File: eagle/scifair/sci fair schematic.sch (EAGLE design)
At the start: 19 parts, among them IC1 LM555N, IC2 LM340H-12, Q1 BC817-16W, Q2 BC817-16W, X1 RIGHT, X2 LEFT, X3 PWR

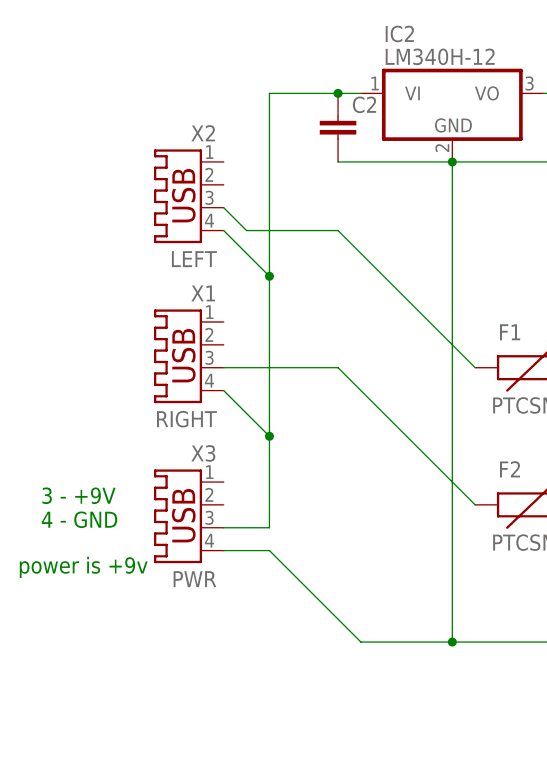
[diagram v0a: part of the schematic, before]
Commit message: Rework USB connections to use Sparkfun breakouts due to resource unavailability
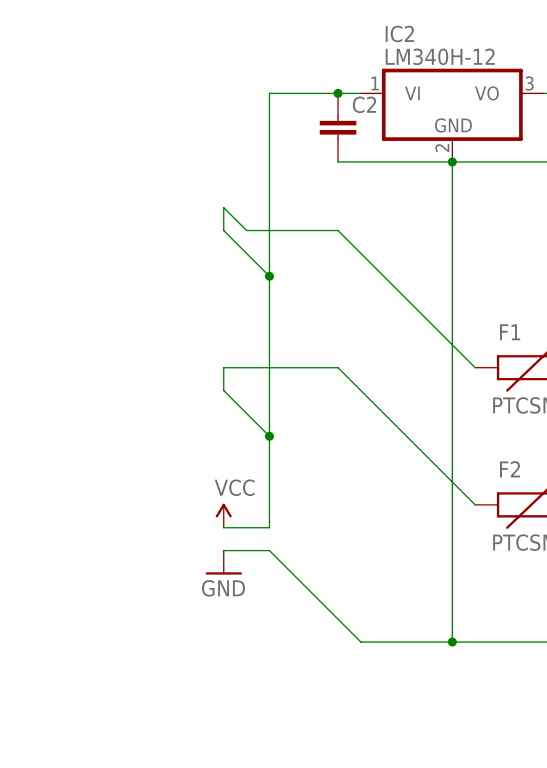
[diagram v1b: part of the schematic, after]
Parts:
- removed X1: RIGHT, con-yamaichi:USB-A003
- removed X2: LEFT, con-yamaichi:USB-A003
- removed X3: PWR, con-yamaichi:USB-A003
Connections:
- net N$6 renamed 5V
- removed net N$1: C2.1, IC2.VI, X1.4, X2.4, X3.3
- removed net N$2: F1.1, X2.3
- removed net N$3: F2.1, X1.3
- new net VCC: C2.1, F1.1, F2.1, IC2.VI
- net GND: no longer X3.4
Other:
- note removed: "3 - +9V 4 - GND"
- note removed: "power is +9v"
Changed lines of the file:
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@@
 <part name="Q1" library="semicon-smd-ipc" deviceset="NPN-TRANSISTOR_" device="SOT23" value="BC817-16W"/>
 <part name="Q2" library="semicon-smd-ipc" deviceset="NPN-TRANSISTOR_" device="SOT23" value="BC817-16W"/>
-<part name="X2" library="con-yamaichi" deviceset="USB-A003" device="" value="LEFT"/>
 <part name="SG2" library="buzzer" deviceset="F/QMX" device=""/>
-<part name="X1" library="con-yamaichi" deviceset="USB-A003" device="" value="RIGHT"/>
-<part name="X3" library="con-yamaichi" deviceset="USB-A003" device="" value="PWR"/>
 <part name="LED3" library="led" deviceset="TLLY4400" device=""/>
 <part name="IC1" library="linear" deviceset="*555" device="N" technology="LM"/>
@@
 <part name="F2" library="SparkFun-PowerIC" deviceset="PTC" device="SMD"/>
 <part name="R2" library="SparkFun-Passives" deviceset="RESISTOR" device="PTH-1/2W"/>
+<part name="SUPPLY1" library="SparkFun-Aesthetics" deviceset="VCC" device=""/>
+<part name="GND1" library="SparkFun-Aesthetics" deviceset="GND" device=""/>
 </parts>
 <sheets>
@@
 <plain>
 <text x="30.48" y="-2.54" size="1.778" layer="91">It would be ideal to incorporate a 555 chip to act as a time-delay</text>
-<text x="0" y="50.8" size="1.778" layer="91">power is +9v</text>
-<text x="2.54" y="55.88" size="1.778" layer="91">3 - +9V
-4 - GND</text>
 <text x="96.52" y="106.68" size="1.778" layer="91">100uf</text>
 <text x="134.62" y="60.96" size="1.778" layer="91">47K ohms</text>
@@
 <instance part="Q1" gate="G$1" x="83.82" y="73.66"/>
 <instance part="Q2" gate="G$1" x="83.82" y="58.42"/>
-<instance part="X2" gate="G$1" x="17.78" y="91.44" rot="MR0"/>
 <instance part="SG2" gate="G$1" x="142.24" y="96.52"/>
-<instance part="X1" gate="G$1" x="17.78" y="73.66" rot="MR0"/>
-<instance part="X3" gate="G$1" x="17.78" y="55.88" rot="MR0"/>
 <instance part="LED3" gate="G$1" x="149.86" y="76.2" rot="R90"/>
 <instance part="IC1" gate="A" x="116.84" y="86.36"/>
@@
 <instance part="F2" gate="G$1" x="55.88" y="58.42"/>
 <instance part="R2" gate="G$1" x="142.24" y="76.2"/>
+<instance part="SUPPLY1" gate="G$1" x="22.86" y="55.88"/>
+<instance part="GND1" gate="1" x="22.86" y="50.8"/>
 </instances>
 <busses>
 </busses>
 <nets>
-<net name="N$1" class="0">
-<segment>
-<pinref part="X3" gate="G$1" pin="3"/>
-<wire x1="22.86" y1="55.88" x2="27.94" y2="55.88" width="0.1524" layer="91"/>
-<wire x1="27.94" y1="55.88" x2="27.94" y2="66.04" width="0.1524" layer="91"/>
-<pinref part="X1" gate="G$1" pin="4"/>
-<wire x1="27.94" y1="66.04" x2="22.86" y2="71.12" width="0.1524" layer="91"/>
-<wire x1="27.94" y1="66.04" x2="27.94" y2="83.82" width="0.1524" layer="91"/>
-<pinref part="X2" gate="G$1" pin="4"/>
-<wire x1="27.94" y1="83.82" x2="22.86" y2="88.9" width="0.1524" layer="91"/>
-<junction x="27.94" y="66.04"/>
-<wire x1="27.94" y1="83.82" x2="27.94" y2="104.14" width="0.1524" layer="91"/>
-<wire x1="27.94" y1="104.14" x2="35.56" y2="104.14" width="0.1524" layer="91"/>
-<pinref part="IC2" gate="A" pin="VI"/>
-<pinref part="C2" gate="G$1" pin="1"/>
-<wire x1="35.56" y1="104.14" x2="38.1" y2="104.14" width="0.1524" layer="91"/>
-<junction x="35.56" y="104.14"/>
-<junction x="27.94" y="83.82"/>
-</segment>
-</net>
-<net name="N$2" class="0">
-<segment>
-<pinref part="X2" gate="G$1" pin="3"/>
-<wire x1="22.86" y1="91.44" x2="25.4" y2="88.9" width="0.1524" layer="91"/>
-<wire x1="25.4" y1="88.9" x2="35.56" y2="88.9" width="0.1524" layer="91"/>
-<wire x1="35.56" y1="88.9" x2="50.8" y2="73.66" width="0.1524" layer="91"/>
-<pinref part="F1" gate="G$1" pin="1"/>
-</segment>
-</net>
-<net name="N$3" class="0">
-<segment>
-<pinref part="X1" gate="G$1" pin="3"/>
-<wire x1="22.86" y1="73.66" x2="35.56" y2="73.66" width="0.1524" layer="91"/>
-<wire x1="35.56" y1="73.66" x2="50.8" y2="58.42" width="0.1524" layer="91"/>
-<pinref part="F2" gate="G$1" pin="1"/>
-</segment>
-</net>
 <net name="N$4" class="0">
 <segment>
@@
 <net name="GND" class="0">
 <segment>
-<pinref part="X3" gate="G$1" pin="4"/>
 <wire x1="48.26" y1="43.18" x2="38.1" y2="43.18" width="0.1524" layer="91"/>
 <wire x1="38.1" y1="43.18" x2="27.94" y2="53.34" width="0.1524" layer="91"/>
@@
 <junction x="121.92" y="43.18"/>
 <junction x="154.94" y="76.2"/>
-</segment>
-</net>
-<net name="N$6" class="0">
+<pinref part="GND1" gate="1" pin="GND"/>
+</segment>
+</net>
+<net name="5V" class="0">
 <segment>
 <wire x1="58.42" y1="104.14" x2="60.96" y2="104.14" width="0.1524" layer="91"/>
@@
 </segment>
 </net>
+<net name="VCC" class="0">
+<segment>
+<wire x1="22.86" y1="55.88" x2="27.94" y2="55.88" width="0.1524" layer="91"/>
+<wire x1="27.94" y1="55.88" x2="27.94" y2="66.04" width="0.1524" layer="91"/>
+<wire x1="27.94" y1="66.04" x2="22.86" y2="71.12" width="0.1524" layer="91"/>
+<wire x1="27.94" y1="66.04" x2="27.94" y2="83.82" width="0.1524" layer="91"/>
+<wire x1="27.94" y1="83.82" x2="22.86" y2="88.9" width="0.1524" layer="91"/>
+<junction x="27.94" y="66.04"/>
+<wire x1="27.94" y1="83.82" x2="27.94" y2="104.14" width="0.1524" layer="91"/>
+<wire x1="27.94" y1="104.14" x2="35.56" y2="104.14" width="0.1524" layer="91"/>
+<pinref part="IC2" gate="A" pin="VI"/>
+<pinref part="C2" gate="G$1" pin="1"/>
+<wire x1="35.56" y1="104.14" x2="38.1" y2="104.14" width="0.1524" layer="91"/>
+<junction x="35.56" y="104.14"/>
+<junction x="27.94" y="83.82"/>
+<pinref part="SUPPLY1" gate="G$1" pin="VCC"/>
+<wire x1="22.86" y1="91.44" x2="25.4" y2="88.9" width="0.1524" layer="91"/>
+<wire x1="25.4" y1="88.9" x2="35.56" y2="88.9" width="0.1524" layer="91"/>
+<wire x1="35.56" y1="88.9" x2="50.8" y2="73.66" width="0.1524" layer="91"/>
+<pinref part="F1" gate="G$1" pin="1"/>
+<wire x1="22.86" y1="91.44" x2="22.86" y2="88.9" width="0.1524" layer="91"/>
+<wire x1="22.86" y1="73.66" x2="35.56" y2="73.66" width="0.1524" layer="91"/>
+<wire x1="35.56" y1="73.66" x2="50.8" y2="58.42" width="0.1524" layer="91"/>
+<pinref part="F2" gate="G$1" pin="1"/>
+<wire x1="22.86" y1="71.12" x2="22.86" y2="73.66" width="0.1524" layer="91"/>
+</segment>
+</net>
 </nets>
 </sheet>
@@
 </schematic>
 </drawing>
-<compatibility>
-<note version="6.3" minversion="6.2.2" severity="warning">
-Since Version 6.2.2 text objects can contain more than one line,
-which will not be processed correctly with this version.
-</note>
-</compatibility>
 </eagle>

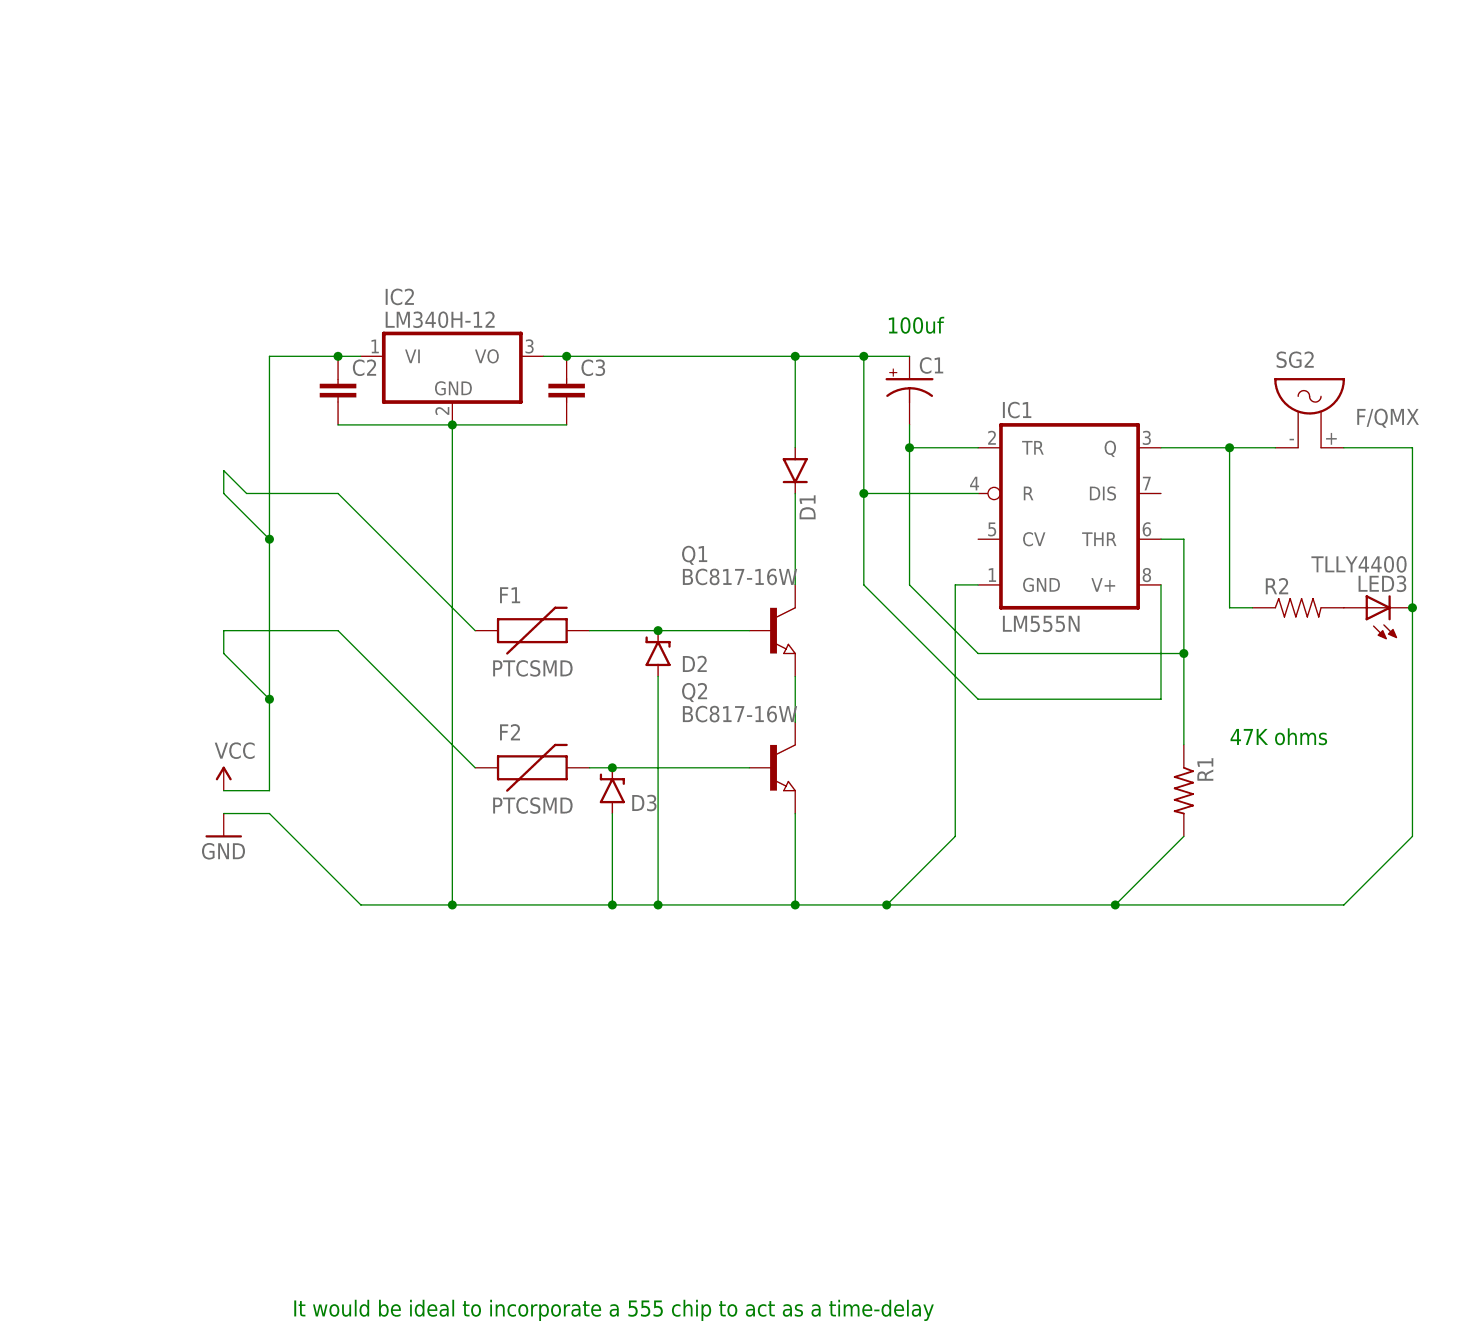
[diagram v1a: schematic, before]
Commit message: Rework board with copper pours and SparkFun USB breakout compatibility
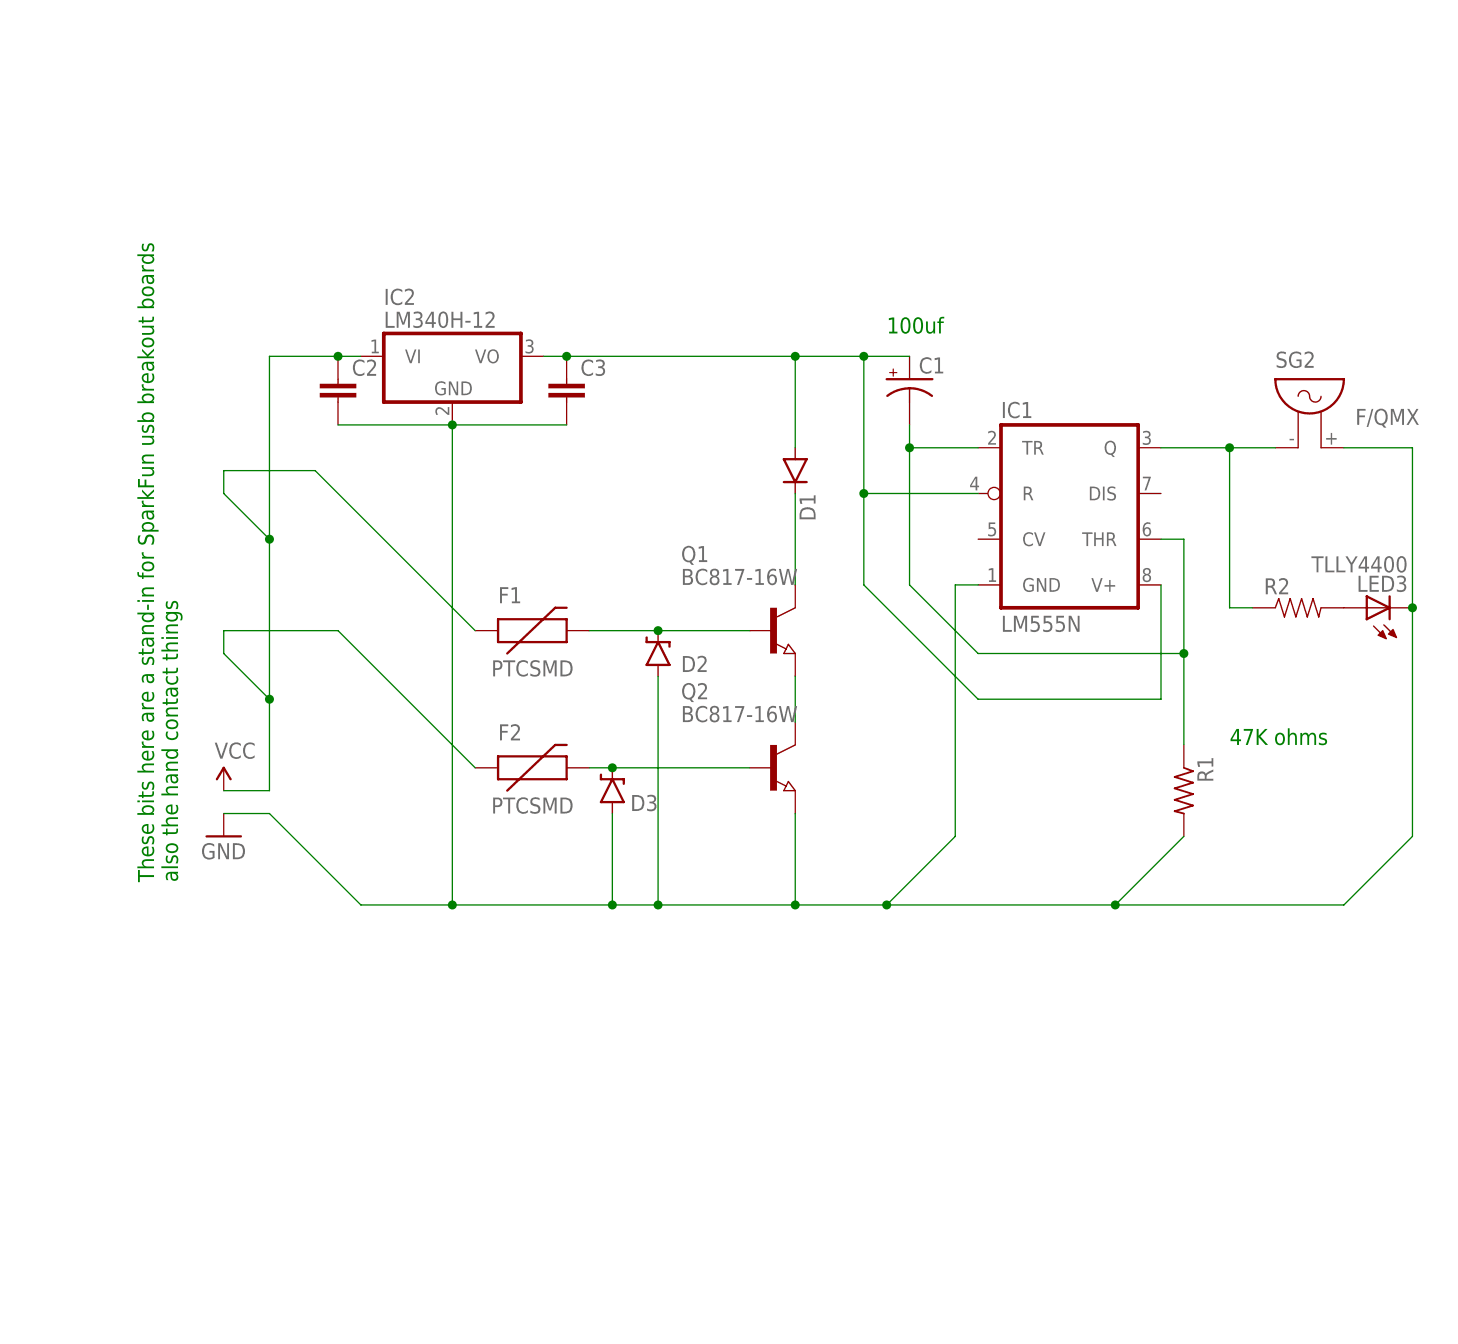
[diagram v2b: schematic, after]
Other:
- note added: "These bits here are a stand-in for SparkFun usb breakout boards also the hand contact things"
- note removed: "It would be ideal to incorporate a 555 chip to act as a time-delay"
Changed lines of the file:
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@@
 <sheet>
 <plain>
-<text x="30.48" y="-2.54" size="1.778" layer="91">It would be ideal to incorporate a 555 chip to act as a time-delay</text>
 <text x="96.52" y="106.68" size="1.778" layer="91">100uf</text>
 <text x="134.62" y="60.96" size="1.778" layer="91">47K ohms</text>
+<text x="17.78" y="45.72" size="1.778" layer="91" rot="R90">These bits here are a stand-in for SparkFun usb breakout boards
+also the hand contact things</text>
 </plain>
 <instances>
@@
 <junction x="27.94" y="83.82"/>
 <pinref part="SUPPLY1" gate="G$1" pin="VCC"/>
-<wire x1="22.86" y1="91.44" x2="25.4" y2="88.9" width="0.1524" layer="91"/>
-<wire x1="25.4" y1="88.9" x2="35.56" y2="88.9" width="0.1524" layer="91"/>
-<wire x1="35.56" y1="88.9" x2="50.8" y2="73.66" width="0.1524" layer="91"/>
+<wire x1="22.86" y1="91.44" x2="33.02" y2="91.44" width="0.1524" layer="91"/>
+<wire x1="33.02" y1="91.44" x2="50.8" y2="73.66" width="0.1524" layer="91"/>
 <pinref part="F1" gate="G$1" pin="1"/>
 <wire x1="22.86" y1="91.44" x2="22.86" y2="88.9" width="0.1524" layer="91"/>
@@
 </schematic>
 </drawing>
+<compatibility>
+<note version="6.3" minversion="6.2.2" severity="warning">
+Since Version 6.2.2 text objects can contain more than one line,
+which will not be processed correctly with this version.
+</note>
+</compatibility>
 </eagle>
